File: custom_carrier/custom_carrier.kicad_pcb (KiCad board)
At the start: 2 copper layers, 2 parts, among them J1 ERF5-040-05.0-X-DV, J2 ERF5-040-05.0-X-DV

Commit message: working on custom carrier in V7
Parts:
- added J3: ERF5-040-05.0-X-DV, pedrolib:SAMTEC_ERF5-040-05.0-X-DV, F.Cu at (103.0, 100.0)
- added J4: ERF5-040-05.0-X-DV, pedrolib:SAMTEC_ERF5-040-05.0-X-DV, F.Cu at (131.5, 117.0)
- added J5: PJ-002AH-SMT-TR, pedrolib:CUI_PJ-002AH-SMT-TR, F.Cu at (100.0, 131.4)
- added J6: 87832-1420, pedrolib:MOLEX_87832-1420, F.Cu at (117.9, 136.8)
- moved J2 29.6 mm to (157.0, 100.0), turned to 90 degrees
- moved J1 11.7 mm to (131.5, 83.0)
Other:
- board outline added: 110 x 90 mm

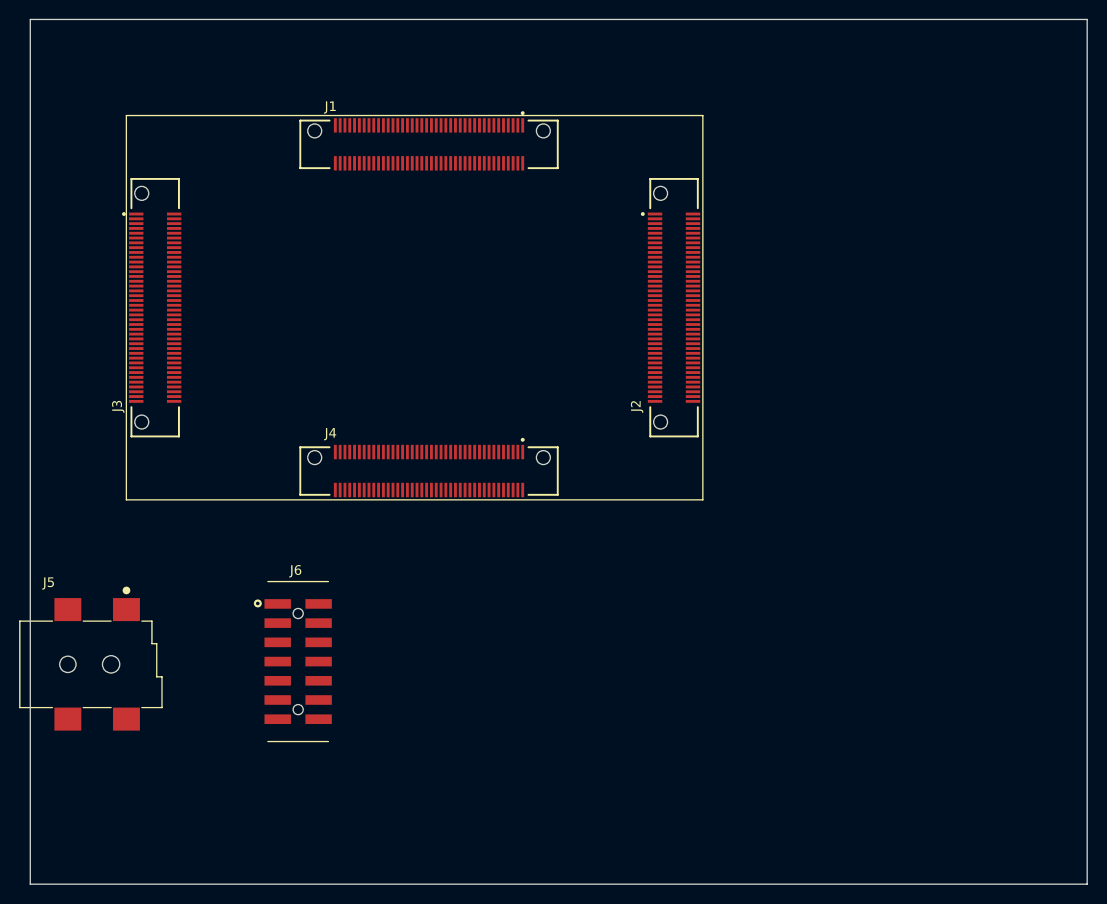
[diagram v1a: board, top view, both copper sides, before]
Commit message: added ribbon cable connectors
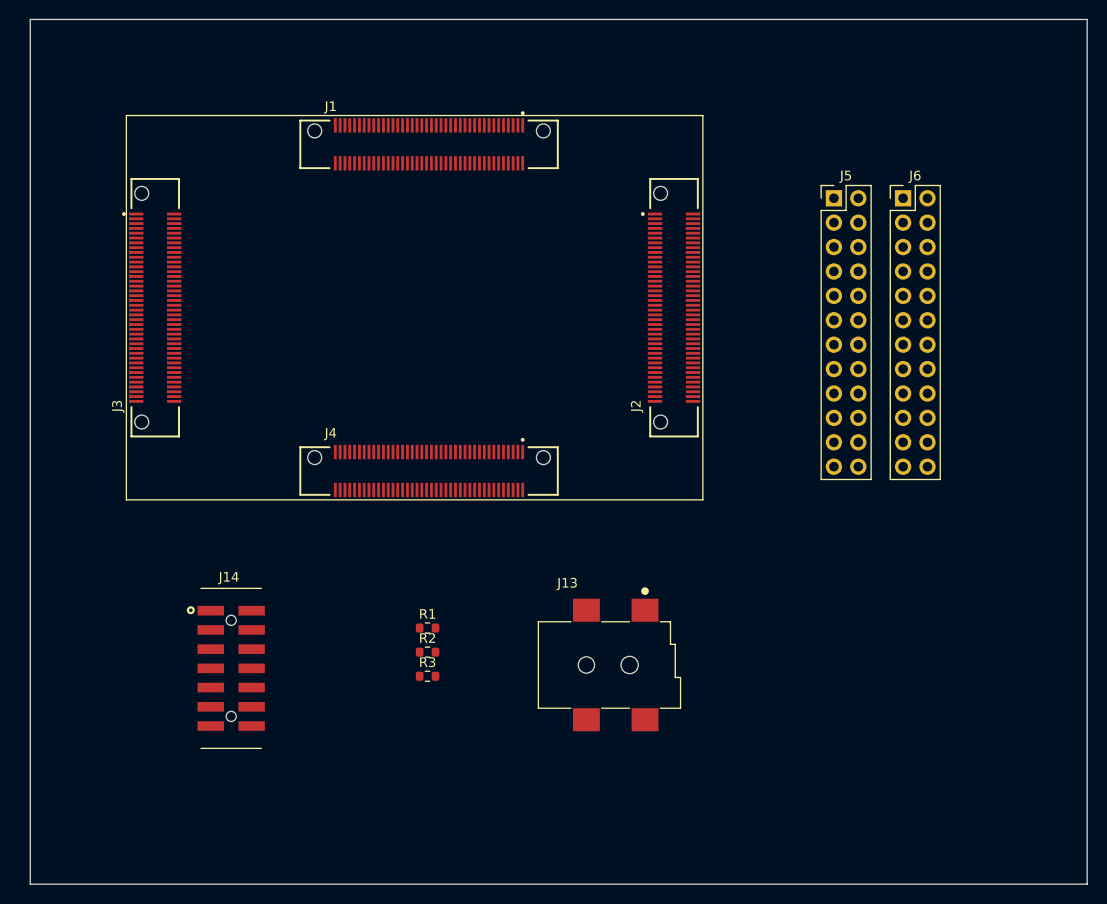
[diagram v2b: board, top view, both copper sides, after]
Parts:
- added J13: PJ-002AH-SMT-TR, pedrolib:CUI_PJ-002AH-SMT-TR, F.Cu at (154.0, 131.5)
- added J14: 87832-1420, pedrolib:MOLEX_87832-1420, F.Cu at (110.9, 137.5)
- added R1: 10K, Resistor_SMD:R_0603_1608Metric, F.Cu at (131.3, 133.3)
- added R2: 10K, Resistor_SMD:R_0603_1608Metric, F.Cu at (131.3, 135.8)
- added R3: 10K, Resistor_SMD:R_0603_1608Metric, F.Cu at (131.3, 138.4)
- J5: value PJ-002AH-SMT-TR -> Conn_02x12_Odd_Even; footprint pedrolib:CUI_PJ-002AH-SMT-TR -> Connector_PinHeader_2.54mm:PinHeader_2x12_P2.54mm_Vertical
- J6: value 87832-1420 -> Conn_02x12_Odd_Even; footprint pedrolib:MOLEX_87832-1420 -> Connector_PinHeader_2.54mm:PinHeader_2x12_P2.54mm_Vertical
- moved J5 85.2 mm to (173.6, 88.6)
- moved J6 79.3 mm to (180.8, 88.6)

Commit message: added 3M connector
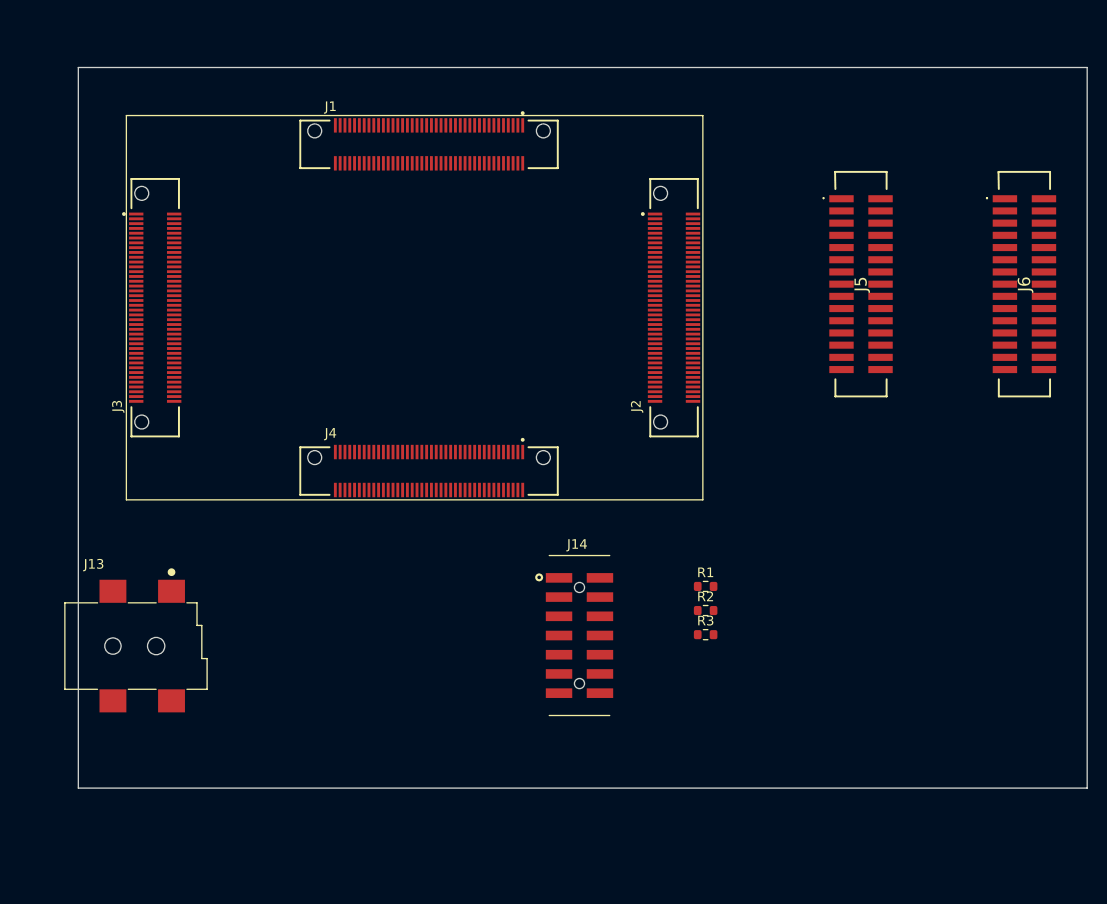
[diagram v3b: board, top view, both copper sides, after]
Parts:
- J5, J6: value Conn_02x12_Odd_Even -> 45230-220230; footprint Connector_PinHeader_2.54mm:PinHeader_2x12_P2.54mm_Vertical -> pedrolib:45230220230
- moved J13 49.3 mm to (104.7, 129.5)
- moved J14 36.4 mm to (147.2, 134.1)
- moved R1 29.3 mm to (160.3, 129.0)
- moved R3 29.3 mm to (160.3, 134.0)
- moved R2 29.3 mm to (160.3, 131.5)
- moved J6 15.5 mm to (193.5, 97.5), turned to -90 degrees
- moved J5 9.37 mm to (176.5, 97.5), turned to -90 degrees
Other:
- board size 110 x 90 mm -> 105 x 75 mm

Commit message: working on high-speed cables.
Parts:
- added C1: 22UF/25V, Capacitor_Tantalum_SMD:CP_EIA-3528-15_AVX-H, F.Cu at (113.3, 129.8)
- added H1: standoff_hole, MountingHole:MountingHole_2.2mm_M2_DIN965_Pad, F.Cu at (103.0, 83.0)
- added H2: standoff_hole, MountingHole:MountingHole_2.2mm_M2_DIN965_Pad, F.Cu at (157.0, 83.0)
- added H3: standoff_hole, MountingHole:MountingHole_2.2mm_M2_DIN965_Pad, F.Cu at (103.0, 117.0)
- added H4: standoff_hole, MountingHole:MountingHole_2.2mm_M2_DIN965_Pad, F.Cu at (157.0, 117.0)
- moved J6 96.9 mm to (108.7, 144.5), turned to 0 degrees
- moved J5 53.8 mm to (151.1, 145.0), turned to 0 degrees
- moved R1 12.1 mm to (150.4, 135.9), turned to 90 degrees
- moved J14 10.9 mm to (156.0, 127.6), turned to 90 degrees
- moved R2 5.98 mm to (156.2, 135.9), turned to -90 degrees
- moved J13 5.57 mm to (104.4, 124.0)
- moved R3 2.34 mm to (161.3, 136.1), turned to -90 degrees
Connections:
- J1 pad 01: unconnected-(J1-Pad01) -> GND
- J1 pad 02: unconnected-(J1-Pad02) -> GND
- J1 pad 11: unconnected-(J1-Pad11) -> GND
- J1 pad 12: unconnected-(J1-Pad12) -> GND
- J1 pad 21: unconnected-(J1-Pad21) -> GND
- J1 pad 22: unconnected-(J1-Pad22) -> GND
- J1 pad 31: unconnected-(J1-Pad31) -> GND
- J1 pad 32: unconnected-(J1-Pad32) -> GND
- J1 pad 41: unconnected-(J1-Pad41) -> GND
- J1 pad 42: unconnected-(J1-Pad42) -> GND
- J1 pad 51: unconnected-(J1-Pad51) -> GND
- J1 pad 52: unconnected-(J1-Pad52) -> GND
- J1 pad 61: unconnected-(J1-Pad61) -> GND
- J1 pad 62: unconnected-(J1-Pad62) -> GND
- J1 pad 64: unconnected-(J1-Pad64) -> +12V
- J1 pad 66: unconnected-(J1-Pad66) -> +12V
- J1 pad 68: unconnected-(J1-Pad68) -> +12V
- J1 pad 70: unconnected-(J1-Pad70) -> GND
- J1 pad 73: unconnected-(J1-Pad73) -> GND
- J1 pad 74: unconnected-(J1-Pad74) -> GND
- J1 pad 75: unconnected-(J1-Pad75) -> +3V3
- J1 pad 76: unconnected-(J1-Pad76) -> +3V3
- J1 pad 79: unconnected-(J1-Pad79) -> GND
- J1 pad 80: unconnected-(J1-Pad80) -> GND
- J13 pad 1A: Net-(J13-Pad1A) -> +12V
- J13 pad 1B: Net-(J13-Pad1A) -> +12V
- J13 pad 2: unconnected-(J13-Pad2) -> GND
- J13 pad 3: unconnected-(J13-Pad3) -> GND
- J2 pad 01: unconnected-(J2-Pad01) -> GND
- J2 pad 02: unconnected-(J2-Pad02) -> GND
- J2 pad 11: unconnected-(J2-Pad11) -> GND
- J2 pad 12: unconnected-(J2-Pad12) -> GND
- J2 pad 21: unconnected-(J2-Pad21) -> GND
- J2 pad 22: unconnected-(J2-Pad22) -> GND
- J2 pad 31: unconnected-(J2-Pad31) -> GND
- J2 pad 32: unconnected-(J2-Pad32) -> GND
- J2 pad 41: unconnected-(J2-Pad41) -> GND
- J2 pad 42: unconnected-(J2-Pad42) -> GND
- J2 pad 51: unconnected-(J2-Pad51) -> GND
- J2 pad 52: unconnected-(J2-Pad52) -> GND
- J2 pad 61: unconnected-(J2-Pad61) -> GND
- J2 pad 62: unconnected-(J2-Pad62) -> GND
- J2 pad 63: unconnected-(J2-Pad63) -> /JTAG_TDI
- J2 pad 65: unconnected-(J2-Pad65) -> /JTAG_TDO
- J2 pad 67: unconnected-(J2-Pad67) -> /JTAG_CLK
- J2 pad 69: unconnected-(J2-Pad69) -> /JTAG_TMS
- J2 pad 73: unconnected-(J2-Pad73) -> GND
- J2 pad 74: unconnected-(J2-Pad74) -> GND
- J2 pad 75: unconnected-(J2-Pad75) -> +3V3
- J2 pad 76: unconnected-(J2-Pad76) -> +3V3
- J2 pad 79: unconnected-(J2-Pad79) -> GND
- J2 pad 80: unconnected-(J2-Pad80) -> GND
- J3 pad 01: unconnected-(J3-Pad01) -> GND
- J3 pad 02: unconnected-(J3-Pad02) -> GND
- J3 pad 07: unconnected-(J3-Pad07) -> GND
- J3 pad 08: unconnected-(J3-Pad08) -> GND
- J3 pad 13: unconnected-(J3-Pad13) -> GND
- J3 pad 14: unconnected-(J3-Pad14) -> GND
- J3 pad 19: unconnected-(J3-Pad19) -> GND
- J3 pad 20: unconnected-(J3-Pad20) -> GND
- J3 pad 25: unconnected-(J3-Pad25) -> GND
- J3 pad 26: unconnected-(J3-Pad26) -> GND
- J3 pad 31: unconnected-(J3-Pad31) -> GND
- J3 pad 32: unconnected-(J3-Pad32) -> GND
- J3 pad 37: unconnected-(J3-Pad37) -> GND
- J3 pad 38: unconnected-(J3-Pad38) -> GND
- J3 pad 43: unconnected-(J3-Pad43) -> GND
- J3 pad 44: unconnected-(J3-Pad44) -> GND
- J3 pad 49: unconnected-(J3-Pad49) -> GND
- J3 pad 50: unconnected-(J3-Pad50) -> GND
- J3 pad 55: unconnected-(J3-Pad55) -> GND
- J3 pad 56: unconnected-(J3-Pad56) -> GND
- J3 pad 61: unconnected-(J3-Pad61) -> GND
- J3 pad 62: unconnected-(J3-Pad62) -> GND
- J3 pad 67: unconnected-(J3-Pad67) -> GND
- J3 pad 68: unconnected-(J3-Pad68) -> GND
- J3 pad 73: unconnected-(J3-Pad73) -> GND
- J3 pad 74: unconnected-(J3-Pad74) -> GND
- J3 pad 79: unconnected-(J3-Pad79) -> GND
- J3 pad 80: unconnected-(J3-Pad80) -> GND
- J4 pad 01: unconnected-(J4-Pad01) -> GND
- J4 pad 02: unconnected-(J4-Pad02) -> GND
- J4 pad 07: unconnected-(J4-Pad07) -> GND
- J4 pad 08: unconnected-(J4-Pad08) -> GND
- J4 pad 10: unconnected-(J4-Pad10) -> /CH1_RX3_P
- J4 pad 12: unconnected-(J4-Pad12) -> /CH1_RX3_N
- J4 pad 13: unconnected-(J4-Pad13) -> GND
- J4 pad 14: unconnected-(J4-Pad14) -> GND
- J4 pad 16: unconnected-(J4-Pad16) -> /CH1_RX2_P
- J4 pad 18: unconnected-(J4-Pad18) -> /CH1_RX2_N
- J4 pad 19: unconnected-(J4-Pad19) -> GND
- J4 pad 20: unconnected-(J4-Pad20) -> GND
- J4 pad 21: unconnected-(J4-Pad21) -> /CH0_DCO_P
- J4 pad 22: unconnected-(J4-Pad22) -> /CH1_RX1_P
- J4 pad 23: unconnected-(J4-Pad23) -> /CH0_DCO_N
- J4 pad 24: unconnected-(J4-Pad24) -> /CH1_RX1_N
- J4 pad 25: unconnected-(J4-Pad25) -> GND
- J4 pad 26: unconnected-(J4-Pad26) -> GND
- J4 pad 27: unconnected-(J4-Pad27) -> /CH0_D3_P
- J4 pad 28: unconnected-(J4-Pad28) -> /CH1_RX0_P
- J4 pad 29: unconnected-(J4-Pad29) -> /CH0_D3_N
- J4 pad 30: unconnected-(J4-Pad30) -> /CH1_RX0_N
- J4 pad 31: unconnected-(J4-Pad31) -> GND
- J4 pad 32: unconnected-(J4-Pad32) -> GND
- J4 pad 33: unconnected-(J4-Pad33) -> /CH0_D2_P
- J4 pad 34: unconnected-(J4-Pad34) -> /CH1_DCO_P
- J4 pad 35: unconnected-(J4-Pad35) -> /CH0_D2_N
- J4 pad 36: unconnected-(J4-Pad36) -> /CH1_DCO_N
- J4 pad 37: unconnected-(J4-Pad37) -> GND
- J4 pad 38: unconnected-(J4-Pad38) -> GND
- J4 pad 39: unconnected-(J4-Pad39) -> /CH0_D1_P
- J4 pad 40: unconnected-(J4-Pad40) -> /CH1_TX3_P
- J4 pad 41: unconnected-(J4-Pad41) -> /CH0_D1_N
- J4 pad 42: unconnected-(J4-Pad42) -> /CH1_TX3_N
- J4 pad 43: unconnected-(J4-Pad43) -> GND
- J4 pad 44: unconnected-(J4-Pad44) -> GND
- J4 pad 45: unconnected-(J4-Pad45) -> /CH0_D0_P
- J4 pad 46: unconnected-(J4-Pad46) -> /CH1_TX2_P
- J4 pad 47: unconnected-(J4-Pad47) -> /CH0_D0_N
- J4 pad 48: unconnected-(J4-Pad48) -> /CH1_TX2_N
- J4 pad 49: unconnected-(J4-Pad49) -> GND
- J4 pad 50: unconnected-(J4-Pad50) -> GND
- J4 pad 51: unconnected-(J4-Pad51) -> /CH0_DCO_P
- J4 pad 52: unconnected-(J4-Pad52) -> /CH1_TX1_P
- J4 pad 53: unconnected-(J4-Pad53) -> /CH0_DCO_N
- J4 pad 54: unconnected-(J4-Pad54) -> /CH1_TX1_N
- J4 pad 55: unconnected-(J4-Pad55) -> GND
- J4 pad 56: unconnected-(J4-Pad56) -> GND
- J4 pad 57: unconnected-(J4-Pad57) -> /CH0_D3_P
- J4 pad 58: unconnected-(J4-Pad58) -> /CH1_TX0_P
- J4 pad 59: unconnected-(J4-Pad59) -> /CH0_D3_N
- J4 pad 60: unconnected-(J4-Pad60) -> /CH1_TX0_N
- J4 pad 61: unconnected-(J4-Pad61) -> GND
- J4 pad 62: unconnected-(J4-Pad62) -> GND
- J4 pad 63: unconnected-(J4-Pad63) -> /CH0_D2_P
- J4 pad 64: unconnected-(J4-Pad64) -> /CH1_CLK_P
- J4 pad 65: unconnected-(J4-Pad65) -> /CH0_D2_N
- J4 pad 66: unconnected-(J4-Pad66) -> /CH1_CLK_N
- J4 pad 67: unconnected-(J4-Pad67) -> GND
- J4 pad 68: unconnected-(J4-Pad68) -> GND
- J4 pad 69: unconnected-(J4-Pad69) -> /CH0_D1_P
- J4 pad 71: unconnected-(J4-Pad71) -> /CH0_D1_N
- J4 pad 73: unconnected-(J4-Pad73) -> GND
- J4 pad 74: unconnected-(J4-Pad74) -> GND
- J4 pad 75: unconnected-(J4-Pad75) -> /CH0_D0_P
- J4 pad 77: unconnected-(J4-Pad77) -> /CH0_D0_N
- J4 pad 79: unconnected-(J4-Pad79) -> GND
- J4 pad 80: unconnected-(J4-Pad80) -> GND
- J5 pad 1: unconnected-(J5-Pad1) -> GND
- J5 pad 10: unconnected-(J5-Pad10) -> /CH1_RX1_N
- J5 pad 11: unconnected-(J5-Pad11) -> GND
- J5 pad 12: unconnected-(J5-Pad12) -> /CH1_RX1_P
- J5 pad 13: unconnected-(J5-Pad13) -> GND
- J5 pad 14: unconnected-(J5-Pad14) -> /CH1_RX2_N
- J5 pad 15: unconnected-(J5-Pad15) -> GND
- J5 pad 16: unconnected-(J5-Pad16) -> /CH1_RX2_P
- J5 pad 17: unconnected-(J5-Pad17) -> GND
- J5 pad 18: unconnected-(J5-Pad18) -> /CH1_RX3_N
- J5 pad 19: unconnected-(J5-Pad19) -> GND
- J5 pad 2: unconnected-(J5-Pad2) -> /CH1_DCO_N
- J5 pad 20: unconnected-(J5-Pad20) -> /CH1_RX3_P
- J5 pad 21: unconnected-(J5-Pad21) -> GND
- J5 pad 23: unconnected-(J5-Pad23) -> GND
- J5 pad 25: unconnected-(J5-Pad25) -> GND
- J5 pad 27: unconnected-(J5-Pad27) -> GND
- J5 pad 29: unconnected-(J5-Pad29) -> GND
- J5 pad 3: unconnected-(J5-Pad3) -> GND
- J5 pad 30: unconnected-(J5-Pad30) -> GND
- J5 pad 4: unconnected-(J5-Pad4) -> /CH1_DCO_P
- J5 pad 5: unconnected-(J5-Pad5) -> GND
- J5 pad 6: unconnected-(J5-Pad6) -> /CH1_RX0_N
- J5 pad 7: unconnected-(J5-Pad7) -> GND
- J5 pad 8: unconnected-(J5-Pad8) -> /CH1_RX0_P
- J5 pad 9: unconnected-(J5-Pad9) -> GND
- J6 pad 1: unconnected-(J6-Pad1) -> GND
- J6 pad 10: unconnected-(J6-Pad10) -> /CH1_TX1_N
- J6 pad 11: unconnected-(J6-Pad11) -> GND
- J6 pad 12: unconnected-(J6-Pad12) -> /CH1_TX1_P
- J6 pad 13: unconnected-(J6-Pad13) -> GND
- J6 pad 14: unconnected-(J6-Pad14) -> /CH1_TX2_N
- J6 pad 15: unconnected-(J6-Pad15) -> GND
- J6 pad 16: unconnected-(J6-Pad16) -> /CH1_TX2_P
- J6 pad 17: unconnected-(J6-Pad17) -> GND
- J6 pad 18: unconnected-(J6-Pad18) -> /CH1_TX3_N
- J6 pad 19: unconnected-(J6-Pad19) -> GND
- J6 pad 2: unconnected-(J6-Pad2) -> /CH1_CLK_N
- J6 pad 20: unconnected-(J6-Pad20) -> /CH1_TX3_P
- J6 pad 21: unconnected-(J6-Pad21) -> GND
- J6 pad 23: unconnected-(J6-Pad23) -> GND
- J6 pad 25: unconnected-(J6-Pad25) -> GND
- J6 pad 27: unconnected-(J6-Pad27) -> GND
- J6 pad 29: unconnected-(J6-Pad29) -> GND
- J6 pad 3: unconnected-(J6-Pad3) -> GND
- J6 pad 30: unconnected-(J6-Pad30) -> GND
- J6 pad 4: unconnected-(J6-Pad4) -> /CH1_CLK_P
- J6 pad 5: unconnected-(J6-Pad5) -> GND
- J6 pad 6: unconnected-(J6-Pad6) -> /CH1_TX0_N
- J6 pad 7: unconnected-(J6-Pad7) -> GND
- J6 pad 8: unconnected-(J6-Pad8) -> /CH1_TX0_P
- J6 pad 9: unconnected-(J6-Pad9) -> GND
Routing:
- net /CH0_D0_N: track 0.00 -> 35.0 mm, vias 0 -> 2
- net /CH0_D0_P: track 0.00 -> 33.9 mm, vias 0 -> 2
- net /CH0_DCO_N: track 0.00 -> 31.3 mm, vias 0 -> 2
- net /CH0_D3_N: track 0.00 -> 31.2 mm, vias 0 -> 2
- net /CH0_DCO_P: track 0.00 -> 30.7 mm, vias 0 -> 2
- net /CH0_D3_P: track 0.00 -> 30.7 mm, vias 0 -> 2
- net /CH0_D1_N: track 0.00 -> 27.5 mm, vias 0 -> 2
- net /CH0_D1_P: track 0.00 -> 26.9 mm, vias 0 -> 2
- net /CH0_D2_P: track 0.00 -> 23.5 mm, vias 0 -> 2
- net /CH0_D2_N: track 0.00 -> 23.2 mm, vias 0 -> 2
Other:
- board size 105 x 75 mm -> 70 x 75 mm
- copper layers 2 -> 4

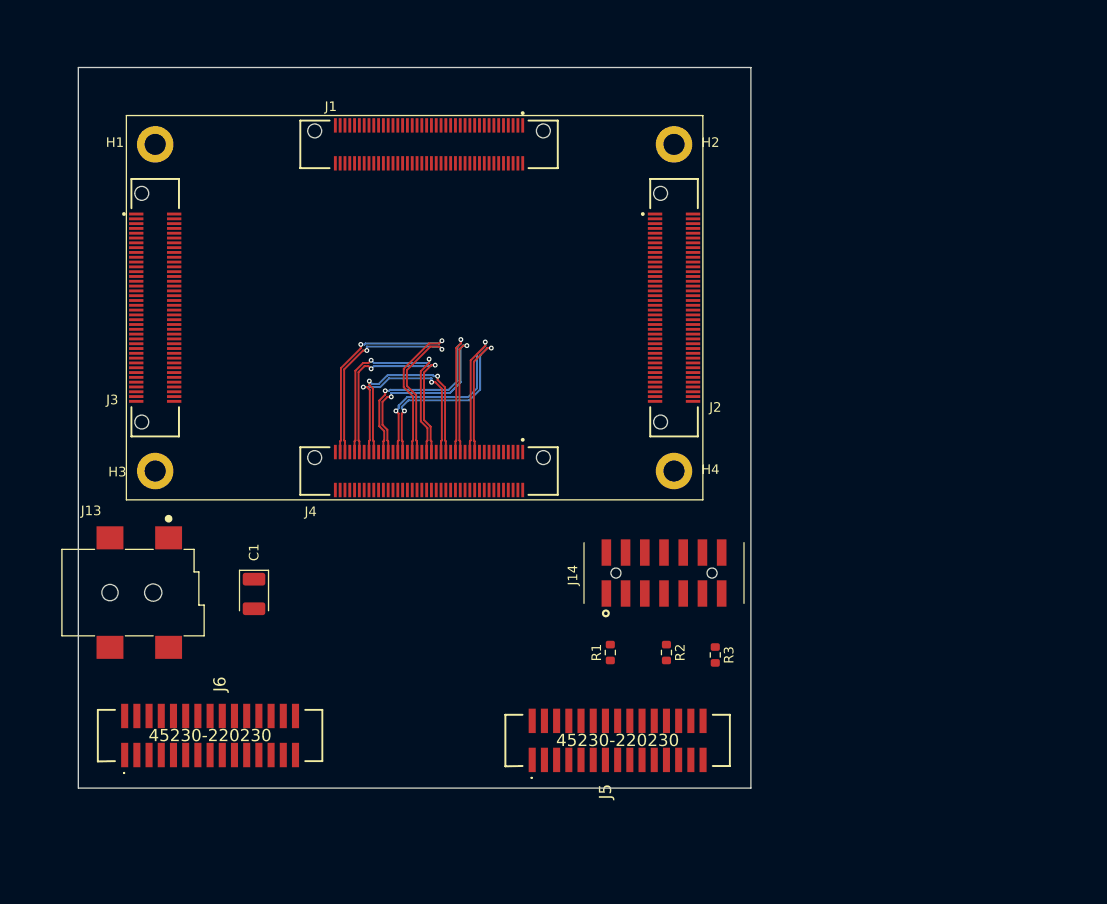
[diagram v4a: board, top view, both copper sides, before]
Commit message: tuned diff lengths and adjusted annular rings
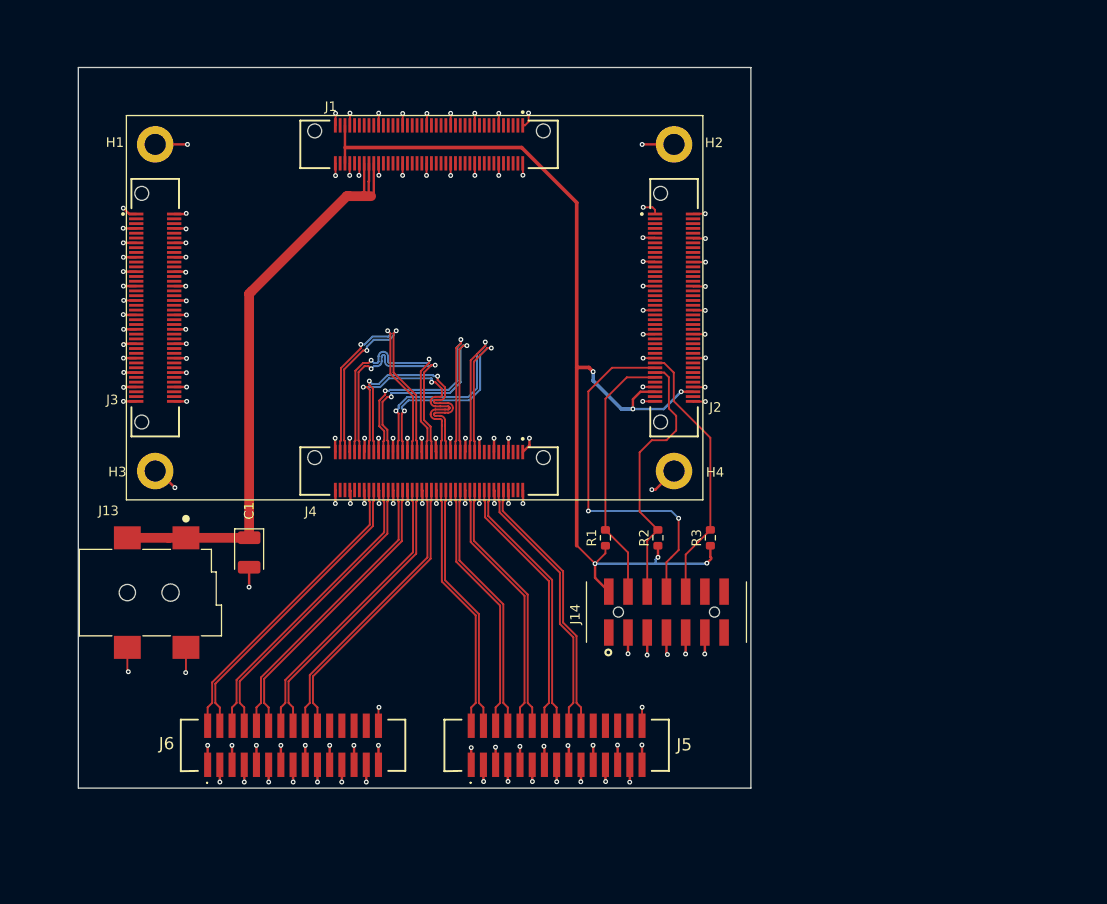
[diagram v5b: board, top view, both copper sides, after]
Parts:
- moved R3 12.2 mm to (160.8, 124.0), turned to 90 degrees
- moved R2 12.0 mm to (155.3, 124.0), turned to 90 degrees
- moved R1 11.9 mm to (149.9, 124.0)
- moved J6 8.70 mm to (117.3, 145.5)
- moved J5 6.37 mm to (144.8, 145.5)
- moved C1 4.35 mm to (112.8, 125.5)
- moved J14 4.07 mm to (156.2, 131.7)
- moved J13 1.81 mm to (106.2, 124.0)
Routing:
- net GND: track 0.00 -> 212.4 mm, vias 0 -> 137
- net +3V3: track 0.00 -> 109.2 mm, vias 0 -> 6
- net +12V: track 0.00 -> 65.6 mm
- net /JTAG_TDO: track 0.00 -> 38.3 mm, vias 0 -> 2
- net /CH1_CLK_N: track 0.00 -> 31.6 mm
- net /CH1_CLK_P: track 0.00 -> 31.6 mm
- net /CH1_TX0_N: track 0.00 -> 31.1 mm
- net /CH1_TX0_P: track 0.00 -> 31.1 mm
- net /CH1_TX1_P: track 0.00 -> 30.7 mm
- net /CH1_TX1_N: track 0.00 -> 30.7 mm
- net /CH1_TX2_N: track 0.00 -> 30.3 mm
- net /CH1_TX2_P: track 0.00 -> 30.3 mm
- net /CH1_TX3_P: track 0.00 -> 29.8 mm
- net /CH1_TX3_N: track 0.00 -> 29.8 mm
- net /JTAG_CLK: track 0.00 -> 28.0 mm
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- added copper zone on In1.Cu, net GND
- added copper zone on In2.Cu, net GND
